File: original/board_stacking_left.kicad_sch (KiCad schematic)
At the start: 52 parts, among them Q1002 MRF9511LT1, Q1004 MRF9511LT1, Q1006 MRF9511LT1, Q1008 MRF9511LT1, Q1010 MRF9511LT1, Q1012 MRF9511LT1, U16 MC100LVEL16, U19 MC100LVEL16, U23 MC100LVEL16

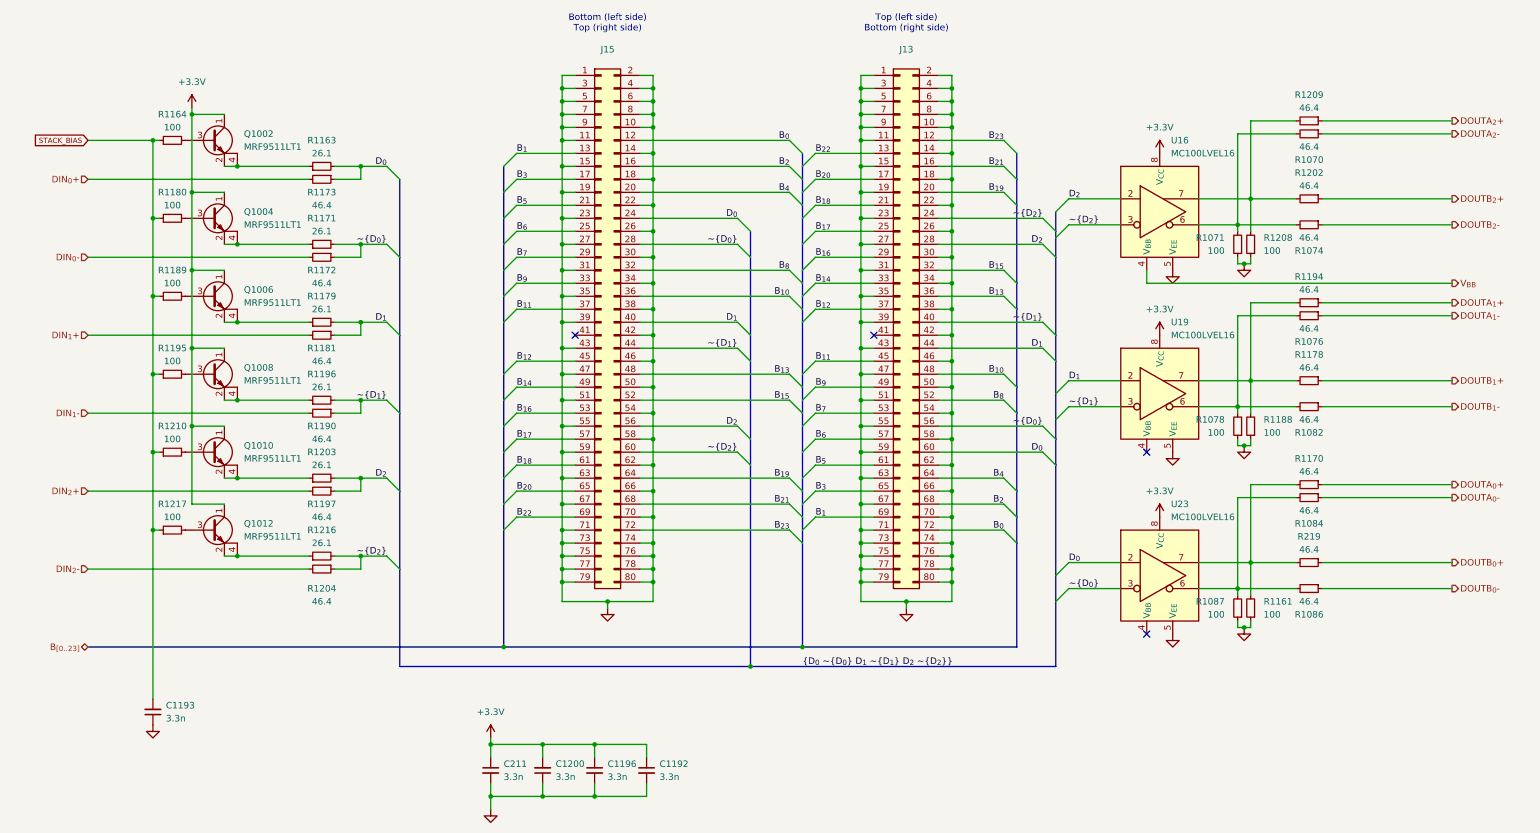
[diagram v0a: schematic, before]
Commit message: clean up routing & add test points on original design
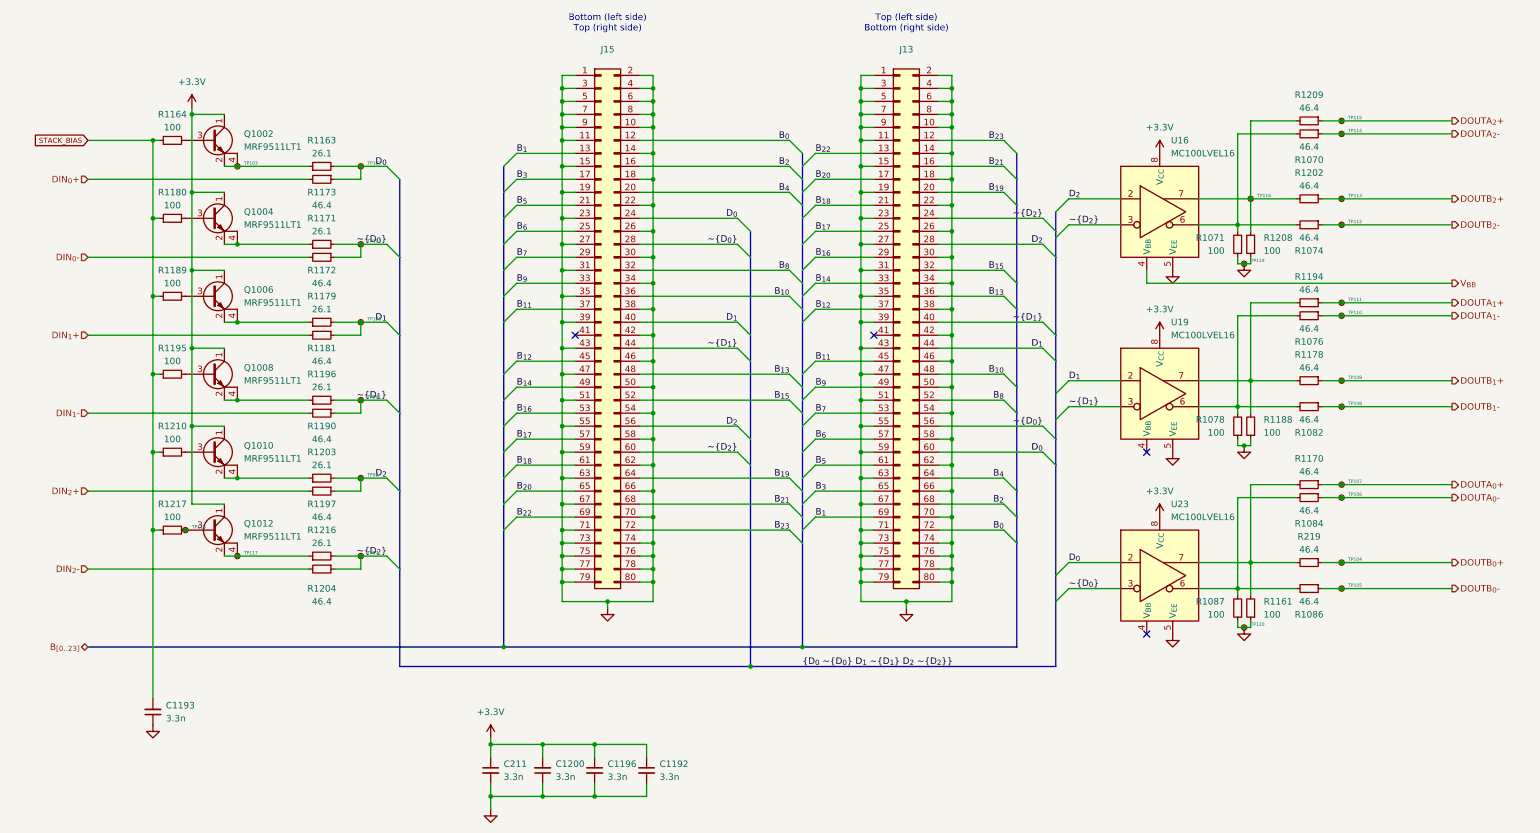
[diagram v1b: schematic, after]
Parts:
- added TP100, TP101, TP102, TP103, TP104, TP105, TP106, TP107, TP108, TP109, TP110, TP111, TP112, TP113, TP114, TP115, TP116, TP117, TP118, TP119, TP120, TP97, TP98, TP99: ~, fp:TestPoint, symbol 16717a:TestPoint_Small
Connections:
- net DOUTA_{0}+: now also TP107.1
- net DOUTA_{0}-: now also TP106.1
- net DOUTA_{1}+: now also TP111.1
- net DOUTA_{1}-: now also TP110.1
- net DOUTA_{2}+: now also TP115.1
- net DOUTA_{2}-: now also TP114.1
- net DOUTB_{0}+: now also TP104.1
- net DOUTB_{0}-: now also TP105.1
- net DOUTB_{1}+: now also TP109.1
- net DOUTB_{1}-: now also TP108.1
- net DOUTB_{2}+: now also TP113.1
- net DOUTB_{2}-: now also TP112.1
- net D_{0}: now also TP102.1
- net D_{1}: now also TP100.1
- net D_{2}: now also TP98.1
- net GND: now also TP119.1, TP120.1
- net ~{D_{0}}: now also TP101.1
- net ~{D_{1}}: now also TP99.1
- net ~{D_{2}}: now also TP97.1
- net at R1202.2, R1208.2, R1209.2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: now also TP116.1
- net at Q1012.2 (E), Q1012.4 (E), R1216.1: now also TP117.1
- net at Q1012.3 (B), R1217.2: now also TP118.1
- net at Q1002.2 (E), Q1002.4 (E), R1163.1: now also TP103.1
